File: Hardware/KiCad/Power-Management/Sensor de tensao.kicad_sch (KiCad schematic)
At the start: 17 parts, among them T1 ZMPT101B, U4 LM358ADE4

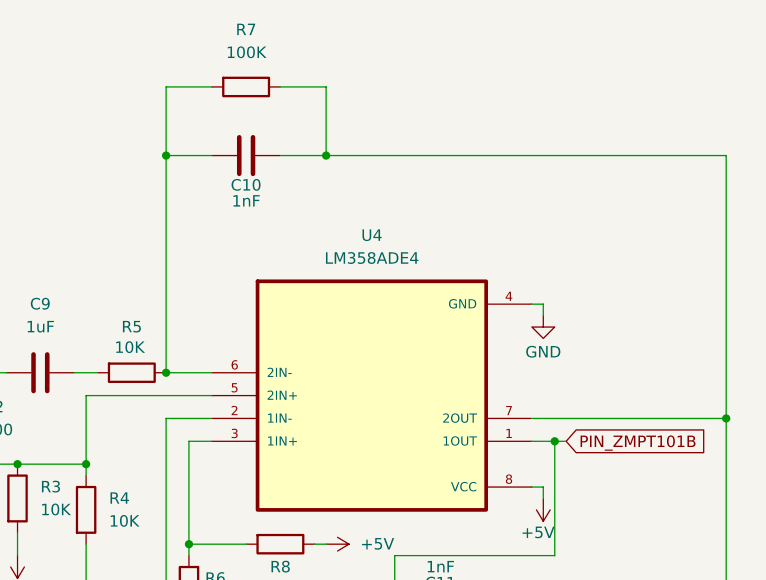
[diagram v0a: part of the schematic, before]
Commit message: troca de sensor de corrente
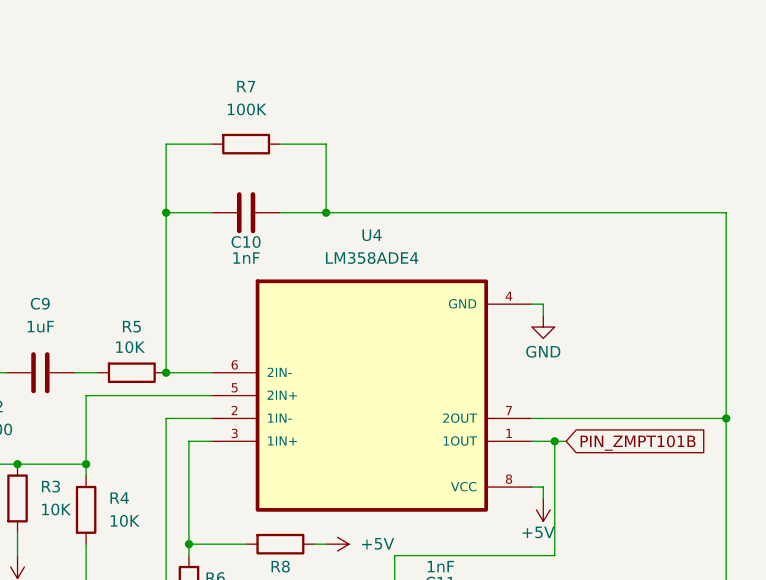
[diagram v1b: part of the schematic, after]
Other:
- moved on the sheet: C10, R7
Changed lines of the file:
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@@
 	)
 	(junction
-		(at 149.86 58.42)
+		(at 149.86 64.77)
 		(diameter 0)
 		(color 0 0 0 0)
@@
 	)
 	(junction
-		(at 132.08 58.42)
+		(at 132.08 64.77)
 		(diameter 0)
 		(color 0 0 0 0)
@@
 	(wire
 		(pts
-			(xy 132.08 58.42) (xy 132.08 50.8)
-		)
-		(stroke
-			(width 0)
-			(type default)
-		)
-	)
-	(wire
-		(pts
-			(xy 194.31 58.42) (xy 194.31 87.63)
+			(xy 132.08 64.77) (xy 132.08 57.15)
+		)
+		(stroke
+			(width 0)
+			(type default)
+		)
+	)
+	(wire
+		(pts
+			(xy 194.31 64.77) (xy 194.31 87.63)
 		)
 		(stroke
@@
 	(wire
 		(pts
-			(xy 144.78 58.42) (xy 149.86 58.42)
-		)
-		(stroke
-			(width 0)
-			(type default)
-		)
-	)
-	(wire
-		(pts
-			(xy 132.08 58.42) (xy 137.16 58.42)
+			(xy 144.78 64.77) (xy 149.86 64.77)
+		)
+		(stroke
+			(width 0)
+			(type default)
+		)
+	)
+	(wire
+		(pts
+			(xy 132.08 64.77) (xy 137.16 64.77)
 		)
 		(stroke
@@
 	(wire
 		(pts
-			(xy 149.86 50.8) (xy 149.86 58.42)
+			(xy 149.86 57.15) (xy 149.86 64.77)
 		)
 		(stroke
@@
 	(wire
 		(pts
-			(xy 144.78 50.8) (xy 149.86 50.8)
+			(xy 144.78 57.15) (xy 149.86 57.15)
 		)
 		(stroke
@@
 	(wire
 		(pts
-			(xy 132.08 50.8) (xy 137.16 50.8)
+			(xy 132.08 57.15) (xy 137.16 57.15)
 		)
 		(stroke
@@
 	(wire
 		(pts
-			(xy 149.86 58.42) (xy 194.31 58.42)
+			(xy 149.86 64.77) (xy 194.31 64.77)
 		)
 		(stroke
@@
 	(wire
 		(pts
-			(xy 132.08 58.42) (xy 132.08 82.55)
+			(xy 132.08 64.77) (xy 132.08 82.55)
 		)
 		(stroke
@@
 	(symbol
 		(lib_id "Device:R")
-		(at 140.97 50.8 270)
+		(at 140.97 57.15 270)
 		(unit 1)
 		(exclude_from_sim no)
@@
 		(fields_autoplaced yes)
 		(property "Reference" "R7"
-			(at 140.97 44.45 90)
+			(at 140.97 50.8 90)
 			(effects
 				(font
@@
 		)
 		(property "Value" "100K"
-			(at 140.97 46.99 90)
+			(at 140.97 53.34 90)
 			(effects
 				(font
@@
 		)
 		(property "Footprint" "Resistor_SMD:R_0805_2012Metric_Pad1.20x1.40mm_HandSolder"
-			(at 140.97 49.022 90)
+			(at 140.97 55.372 90)
 			(effects
 				(font
@@
 		)
 		(property "Datasheet" "~"
-			(at 140.97 50.8 0)
+			(at 140.97 57.15 0)
 			(effects
 				(font
@@
 		)
 		(property "Description" "Resistor"
-			(at 140.97 50.8 0)
+			(at 140.97 57.15 0)
 			(effects
 				(font
@@
 	(symbol
 		(lib_id "Device:C")
-		(at 140.97 58.42 90)
+		(at 140.97 64.77 90)
 		(unit 1)
 		(exclude_from_sim no)
@@
 		(dnp no)
 		(property "Reference" "C10"
-			(at 140.97 61.722 90)
+			(at 140.97 68.072 90)
 			(effects
 				(font
@@
 		)
 		(property "Value" "1nF"
-			(at 140.97 63.5 90)
+			(at 140.97 69.85 90)
 			(effects
 				(font
@@
 		)
 		(property "Footprint" "Capacitor_SMD:C_0805_2012Metric_Pad1.18x1.45mm_HandSolder"
-			(at 144.78 57.4548 0)
+			(at 144.78 63.8048 0)
 			(effects
 				(font
@@
 		)
 		(property "Datasheet" "~"
-			(at 140.97 58.42 0)
+			(at 140.97 64.77 0)
 			(effects
 				(font
@@
 		)
 		(property "Description" "Unpolarized capacitor"
-			(at 140.97 58.42 0)
-			(effects
-				(font
+			(at 140.97 64.77 0)
+			(effects
+				(font
